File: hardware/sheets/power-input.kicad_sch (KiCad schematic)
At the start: 9 parts, among them J21 KPJX-4S-S, Q20 AO4407A

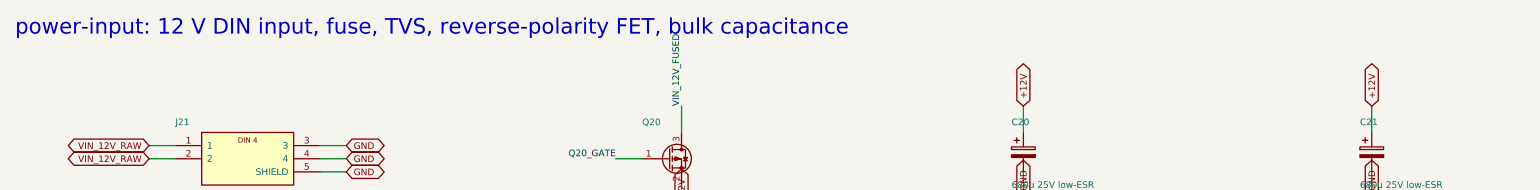
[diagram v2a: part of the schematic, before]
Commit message: docs: C24 brain + bay cards — decisions, architecture, BOM card table, fabrication, README, USAGE, STATUS, changelog, history; diagrams: 8 slots, lid plan, left wall
Co-Authored-By: Claude Fable 5.1 <noreply@anthropic.com>
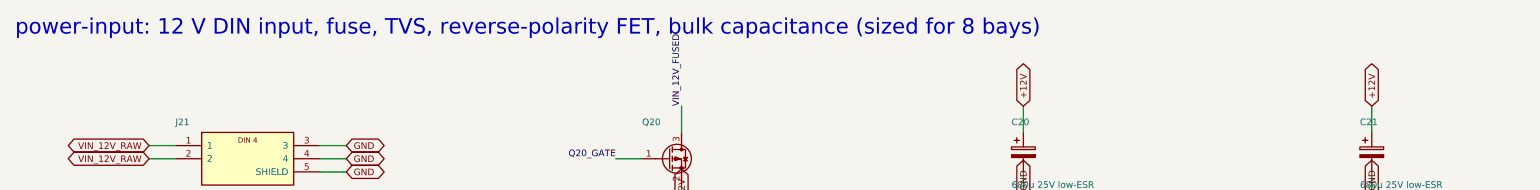
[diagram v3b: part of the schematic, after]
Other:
- note added: "power-input: 12 V DIN input, fuse, TVS, reverse-polarity FET, bulk capacitance (sized for 8 bays)"
- note removed: "power-input: 12 V DIN input, fuse, TVS, reverse-polarity FET, bulk capacitance"
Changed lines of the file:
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@@
 		(company "brain-drain")
 	)
-	(text "power-input: 12 V DIN input, fuse, TVS, reverse-polarity FET, bulk capacitance"
+	(text "power-input: 12 V DIN input, fuse, TVS, reverse-polarity FET, bulk capacitance (sized for 8 bays)"
 		(exclude_from_sim no)
 		(at 30 12 0)

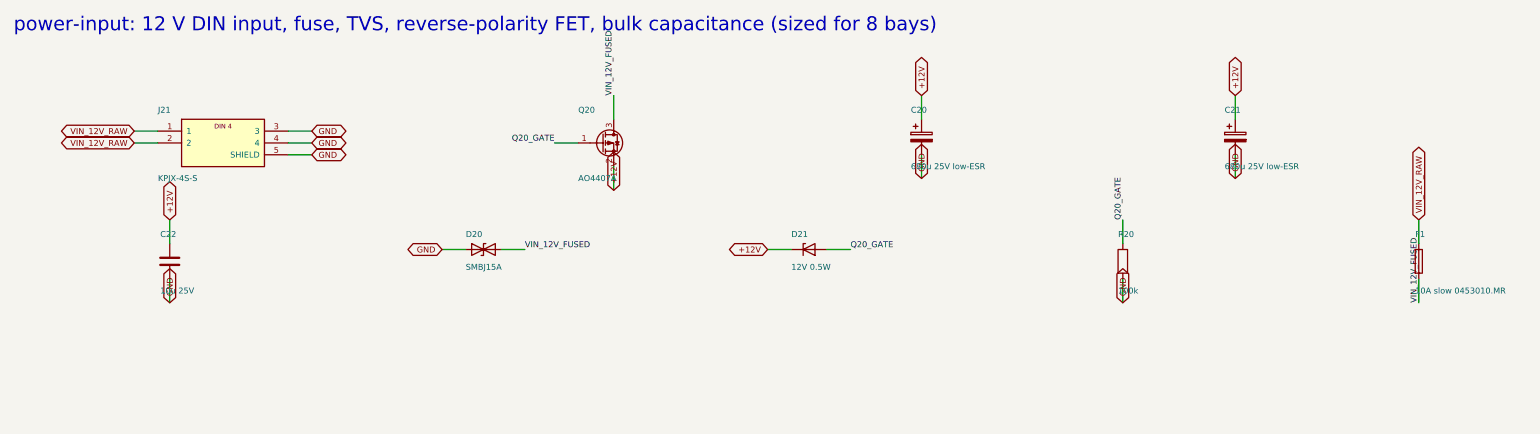
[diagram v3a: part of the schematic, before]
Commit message: hw: 8-pin P-FET symbols (S 1-3, G 4, D 5-8 + EP) for Q20 / Q1 / Q2 — the generic 3-pin symbol had put G/S/D on three source pads; route.py update-nets re-syncs pad nets on a routed board; gen_sch keeps the board design rules; rules restored in both projects
Co-Authored-By: Claude Fable 5.1 <noreply@anthropic.com>
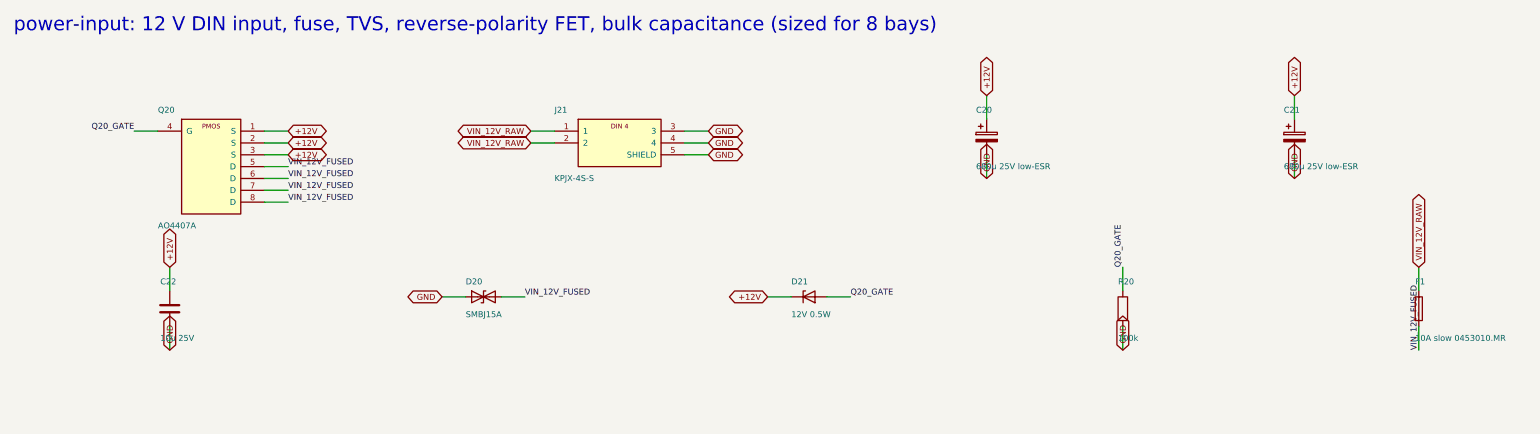
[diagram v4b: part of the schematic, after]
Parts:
- J21: renamed from Q20; value AO4407A -> KPJX-4S-S; footprint Package_SO:SOIC-8_3.9x4.9mm_P1.27mm -> brain-drain:Kycon_KPJX-4S-S; symbol Transistor_FET:Q_PMOS_GSD -> brain-drain:DIN4_KPJX
- Q20: renamed from J21; value KPJX-4S-S -> AO4407A; footprint brain-drain:Kycon_KPJX-4S-S -> Package_SO:SOIC-8_3.9x4.9mm_P1.27mm; symbol brain-drain:DIN4_KPJX -> brain-drain:PMOS_SSSGDDDD
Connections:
- net +12V: now also Q20.1 (S), Q20.2 (S), Q20.3 (S); no longer J21.2 (S)
- net GND: now also J21.3, J21.4, J21.5 (SHIELD); no longer Q20.3, Q20.4, Q20.5 (SHIELD)
- net Q20_GATE: now also Q20.4 (G); no longer J21.1 (G)
- net VIN_12V_FUSED: now also Q20.5 (D), Q20.6 (D), Q20.7 (D), Q20.8 (D); no longer J21.3 (D)
- net VIN_12V_RAW: now also J21.1, J21.2; no longer Q20.1, Q20.2
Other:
- moved on the sheet: C20, C21, C22, D20, D21, F1, R20

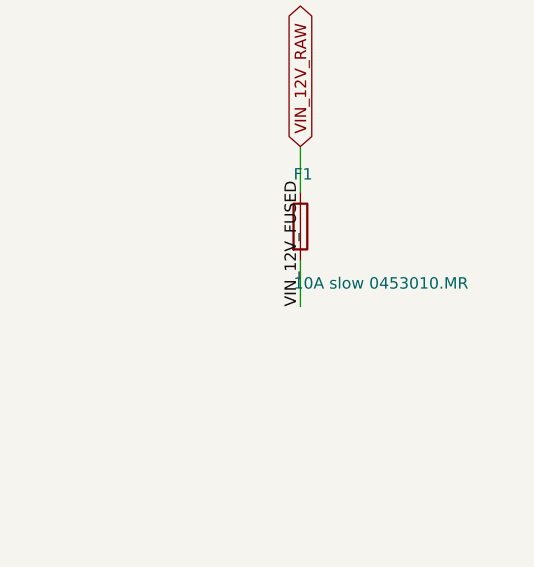
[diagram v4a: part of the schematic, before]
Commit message: hw: input fuse F1 15 A slow-blow (C31); BOM, netlist and docs updated
Co-Authored-By: Claude Sonnet 5 <noreply@anthropic.com>
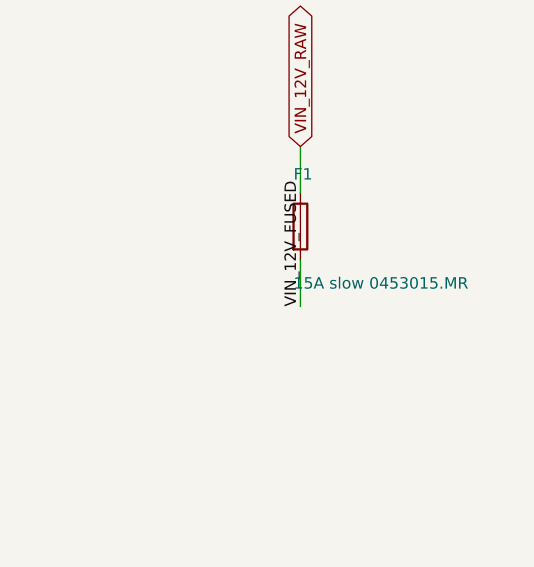
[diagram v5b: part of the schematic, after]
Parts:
- F1: value 10A slow 0453010.MR -> 15A slow 0453015.MR
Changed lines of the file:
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@@
 			)
 		)
-		(property "Value" "10A slow 0453010.MR"
+		(property "Value" "15A slow 0453015.MR"
 			(at 330.708 77.43 0)
 			(effects
